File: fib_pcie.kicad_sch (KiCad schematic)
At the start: 57 parts, among them J901 Bus_M.2_2199230-6, J902 Bus_M.2_1-2199230-6, M901 Mech_M2_2280_H2.5mm, Y901 Oscillator_SMD_32.768kHz_ECS_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

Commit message: added some missing footprints, stared working ono power-on and sequencing
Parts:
- C917: value C_100n_0402 -> 100nF; footprint jetson-orin-baseboard-footprints:C_0402_1005Metric -> Capacitor_SMD:C_0603_1608Metric
- R913, R914, R919, R920, R921, R922, R923: footprint jetson-orin-baseboard-footprints:R_0402_1005Metric -> Resistor_SMD:R_0603_1608Metric
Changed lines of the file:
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@@
 			)
 		)
-		(property "Footprint" "jetson-orin-baseboard-footprints:R_0402_1005Metric"
+		(property "Footprint" "Resistor_SMD:R_0603_1608Metric"
 			(at 175.26 151.13 0)
 			(effects
@@
 			)
 		)
-		(property "Footprint" "jetson-orin-baseboard-footprints:R_0402_1005Metric"
+		(property "Footprint" "Resistor_SMD:R_0603_1608Metric"
 			(at 251.46 153.67 0)
 			(effects
@@
 			)
 		)
-		(property "Footprint" "jetson-orin-baseboard-footprints:R_0402_1005Metric"
+		(property "Footprint" "Resistor_SMD:R_0603_1608Metric"
 			(at 175.26 158.75 0)
 			(effects
@@
 			)
 		)
-		(property "Footprint" "jetson-orin-baseboard-footprints:R_0402_1005Metric"
+		(property "Footprint" "Resistor_SMD:R_0603_1608Metric"
 			(at 175.26 146.05 0)
 			(effects
@@
 			)
 		)
-		(property "Footprint" "jetson-orin-baseboard-footprints:R_0402_1005Metric"
+		(property "Footprint" "Resistor_SMD:R_0603_1608Metric"
 			(at 251.46 163.83 0)
 			(effects
@@
 			)
 		)
-		(property "Footprint" "jetson-orin-baseboard-footprints:R_0402_1005Metric"
+		(property "Footprint" "Resistor_SMD:R_0603_1608Metric"
 			(at 175.26 148.59 0)
 			(effects
@@
 			)
 		)
-		(property "Footprint" "jetson-orin-baseboard-footprints:R_0402_1005Metric"
+		(property "Footprint" "Resistor_SMD:R_0603_1608Metric"
 			(at 251.46 158.75 0)
 			(effects
@@
 			)
 		)
-		(property "Value" "C_100n_0402"
+		(property "Value" "100nF"
 			(at 34.29 176.53 0)
 			(effects
@@
 			)
 		)
-		(property "Footprint" "jetson-orin-baseboard-footprints:C_0402_1005Metric"
+		(property "Footprint" "Capacitor_SMD:C_0603_1608Metric"
 			(at 36.83 176.53 0)
 			(effects

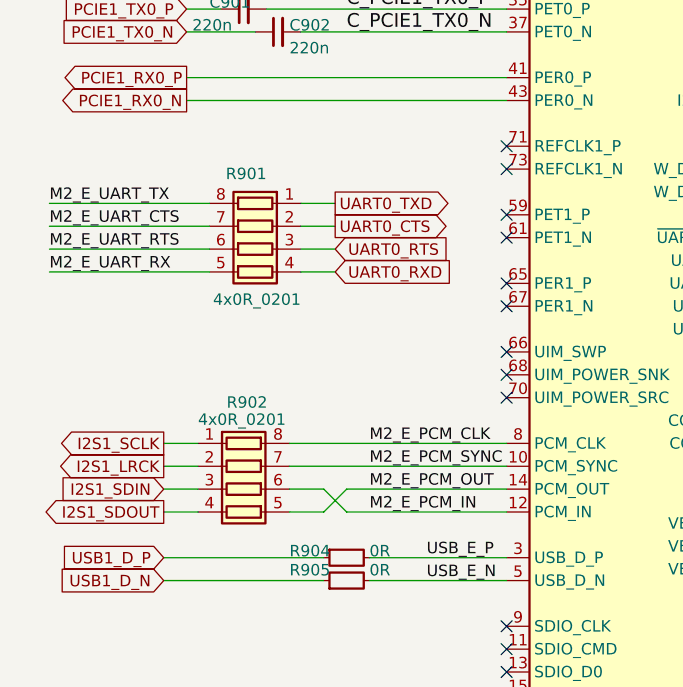
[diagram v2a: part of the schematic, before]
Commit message: implemented most of USB and Power Supplies
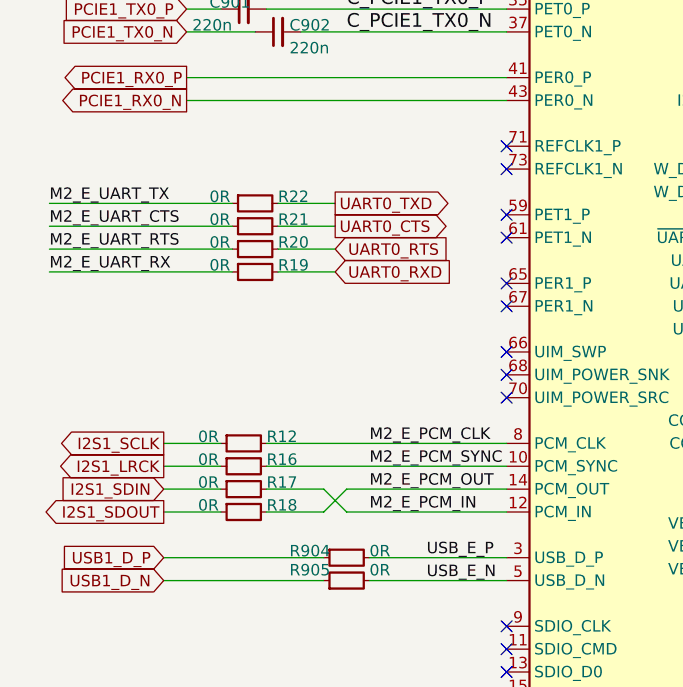
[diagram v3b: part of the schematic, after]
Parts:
- removed R901, R902: R_4x0R_0201_array, jetson-orin-baseboard-footprints:R_Array_4x0201_Panasonic_EXB18V, symbol jetson-orin-baseboard:R_4x0R_0201_array
- added R12, R16, R17, R18, R19, R20, R21, R22: R_0R_0402, Resistor_SMD:R_0402_1005Metric, symbol jetson-orin-baseboard:R_0R_0402
- C901, C902, C905, C906, C907, C908, C909, C910, C911, C912, C917: footprint Capacitor_SMD:C_0603_1608Metric -> Capacitor_SMD:C_0402_1005Metric
- R903, R904, R905, R906, R907, R908, R909, R910, R911, R912, R913, R914, R915, R916, R917, R918, R919, R920, R921, R922, R923: footprint Resistor_SMD:R_0603_1608Metric -> Resistor_SMD:R_0402_1005Metric
- TP901, TP902, TP903, TP904, TP905, TP906, TP907: footprint TestPoint:TestPoint_Pad_D1.0mm -> (none)
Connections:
- net I2S1_LRCK: now also R16.1
- net I2S1_SCLK: now also R12.1
- net I2S1_SDIN: now also R17.1
- net I2S1_SDOUT: now also R18.1
- net M2_E_PCM_CLK: now also R12.2
- net M2_E_PCM_IN: now also R17.2
- net M2_E_PCM_OUT: now also R18.2
- net M2_E_PCM_SYNC: now also R16.2
- net M2_E_UART_CTS: now also R21.1
- net M2_E_UART_RTS: now also R20.1
- net M2_E_UART_RX: now also R19.1
- net M2_E_UART_TX: now also R22.1
- net UART0_CTS: now also R21.2
- net UART0_RTS: now also R20.2
- net UART0_RXD: now also R19.2
- net UART0_TXD: now also R22.2

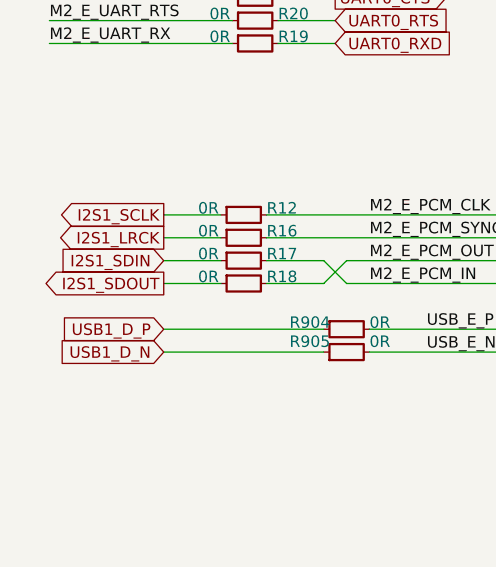
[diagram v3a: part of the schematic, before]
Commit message: did a big portion of pcie, optimized placement of components and subsections. power, usb and charging is largely done. still need to do length matching though. will need to take a second look at schemativs after routing is done
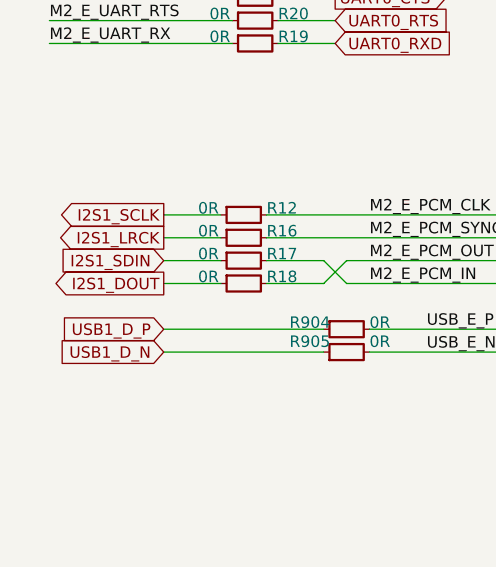
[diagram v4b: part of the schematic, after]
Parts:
- J901: footprint jetson-orin-baseboard-footprints:Bus_M.2_Socket_Key_E_TE_2199230-6 -> Fibel2:21992306; symbol jetson-orin-baseboard:Bus_M.2_2199230-6 -> Fibel2:Bus_M.2_2199230-6
- J902: footprint jetson-orin-baseboard-footprints:Bus_M.2_Socket_Key_M_TE_1-2199230-6 -> Fibel2:121992306; symbol jetson-orin-baseboard:Bus_M.2_1-2199230-6 -> Fibel2:Bus_M.2_1-2199230-6
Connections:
- net I2S1_SDOUT renamed I2S1_DOUT
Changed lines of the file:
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@@
 		)
 	)
-	(global_label "I2S1_SDOUT"
+	(global_label "I2S1_DOUT"
 		(shape output)
 		(at 30.48 105.41 180)
@@
 	)
 	(symbol
-		(lib_id "jetson-orin-baseboard:Bus_M.2_2199230-6")
+		(lib_id "Fibel2:Bus_M.2_2199230-6")
 		(at 68.58 31.75 0)
 		(unit 1)
@@
 			)
 		)
-		(property "Footprint" "jetson-orin-baseboard-footprints:Bus_M.2_Socket_Key_E_TE_2199230-6"
+		(property "Footprint" "Fibel2:21992306"
 			(at 114.3 38.1 0)
 			(effects
@@
 	)
 	(symbol
-		(lib_id "jetson-orin-baseboard:Bus_M.2_1-2199230-6")
+		(lib_id "Fibel2:Bus_M.2_1-2199230-6")
 		(at 200.66 38.1 0)
 		(unit 1)
@@
 			)
 		)
-		(property "Footprint" "jetson-orin-baseboard-footprints:Bus_M.2_Socket_Key_M_TE_1-2199230-6"
+		(property "Footprint" "Fibel2:121992306"
 			(at 246.38 48.26 0)
 			(effects

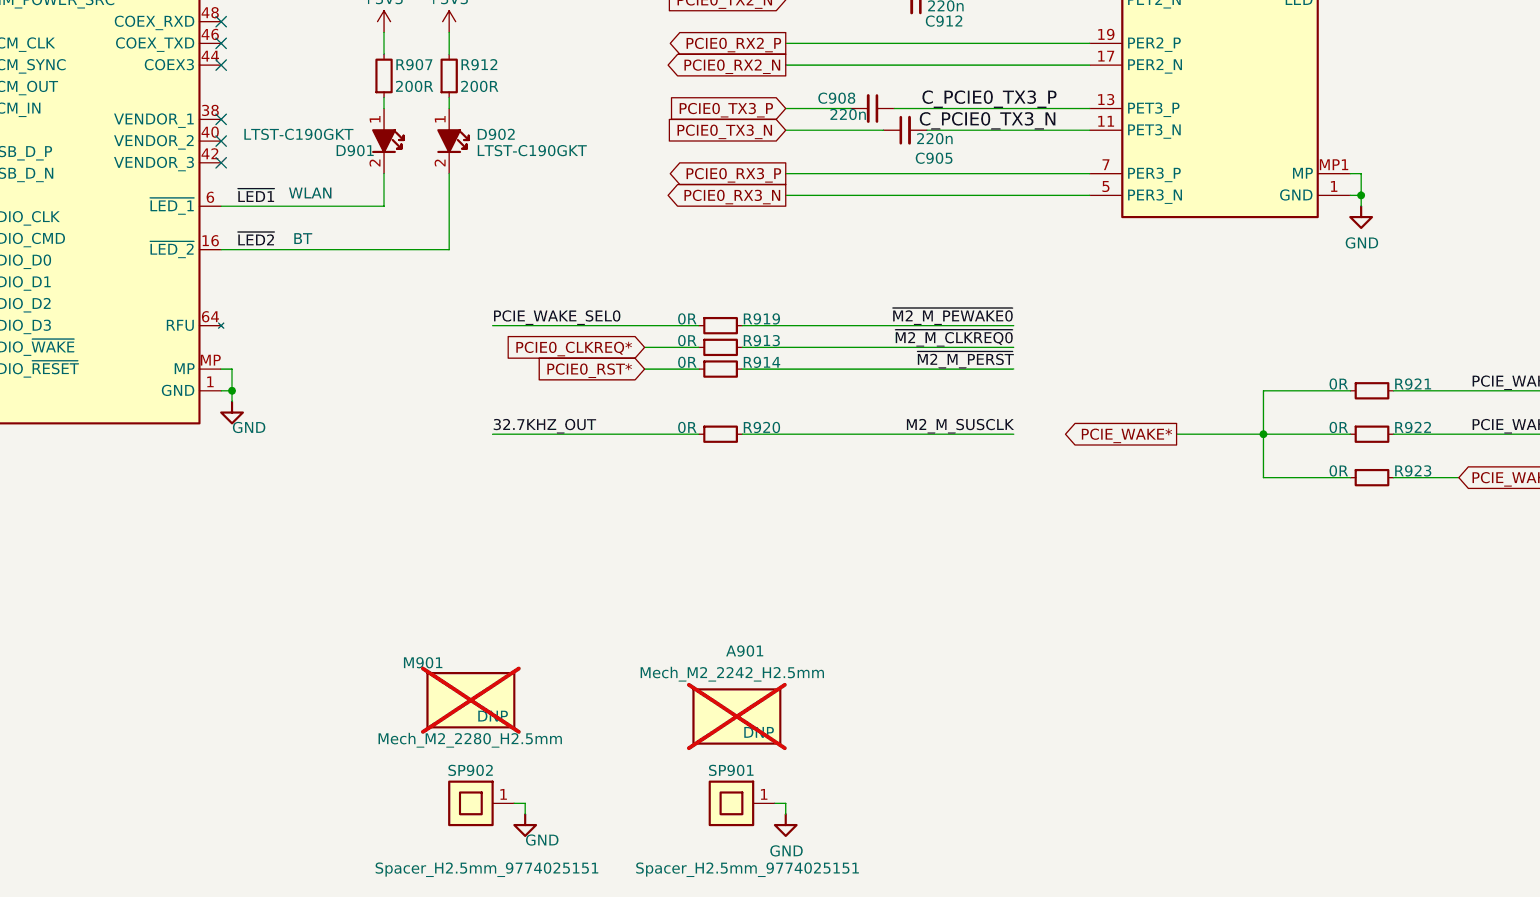
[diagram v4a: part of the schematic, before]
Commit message: further optimized placement, finished most of buck array, expanded pcie, added tons of missing footprints, diff pair spacing optimization
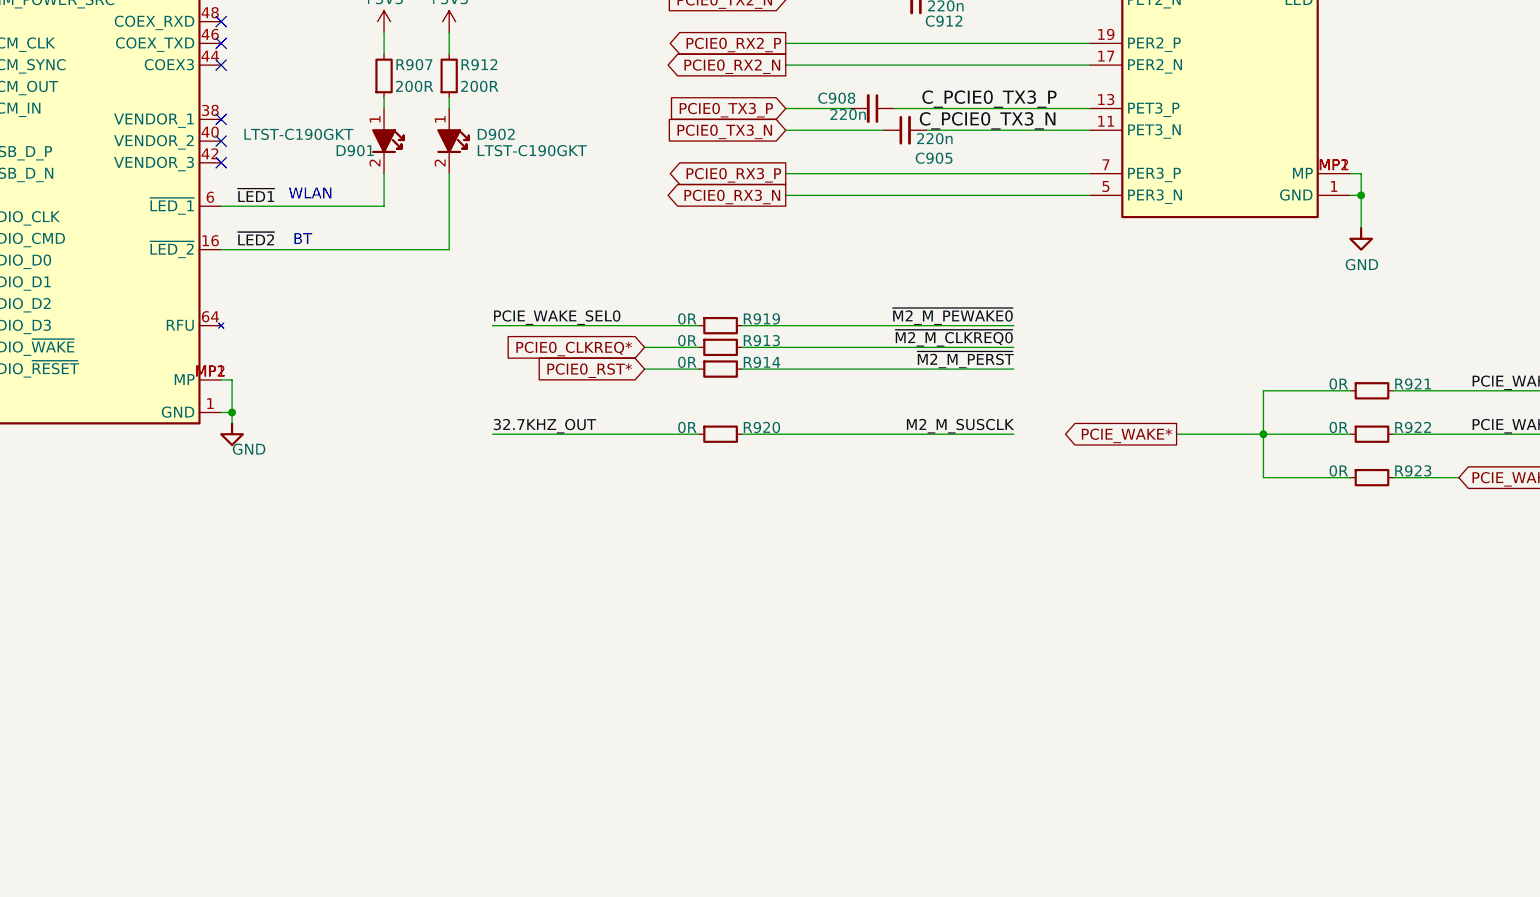
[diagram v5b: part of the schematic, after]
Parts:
- removed A901: Mech_M2_2242_H2.5mm, jetson-orin-baseboard-footprints:Mech_M2_2242_H2.5mm, symbol jetson-orin-baseboard:Mech_M2_2242_H2.5mm
- removed M901: Mech_M2_2280_H2.5mm, jetson-orin-baseboard-footprints:Mech_M2_2280_H2.5mm, symbol jetson-orin-baseboard:Mech_M2_2280_H2.5mm
- removed SP901, SP902: Spacer_H2.5mm_9774025151, jetson-orin-baseboard-footprints:Spacer_Drill3.7mm_H2.5mm_9774025151R, symbol jetson-orin-baseboard:Spacer_Drill3.7mm_H2.5mm_9774025151R
- D901, D902, D903: footprint jetson-orin-baseboard-footprints:LED_0603_1608Metric_G -> LED_SMD:LED_0603_1608Metric
- TP901, TP902, TP903, TP904, TP905, TP906, TP907: footprint (none) -> TestPoint:TestPoint_Pad_D1.0mm
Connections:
- net GND: now also J901.MP1 (MP), J901.MP2 (MP); no longer J901.MP

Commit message: 90 percent done with routing. need to go over all schematic pages, double check everything thoroughly, do lengthmatching add any missing footprints, take care of startup, ferrites, audio, eink connectors, 40pin header connections, rtc
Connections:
- net +3V3: no longer R917.2
- net 3V3_M2: now also R917.2
- net SYS_SCL renamed PCIE_SCL
- net SYS_SDA renamed PCIE_SDA
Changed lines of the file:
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@@
 	(wire
 		(pts
-			(xy 232.41 76.2) (xy 232.41 77.47)
+			(xy 232.41 74.93) (xy 232.41 77.47)
 		)
 		(stroke
@@
 		)
 	)
+	(label "3V3_M2"
+		(at 232.41 74.93 0)
+		(fields_autoplaced yes)
+		(effects
+			(font
+				(size 1.27 1.27)
+			)
+			(justify left bottom)
+		)
+	)
 	(label "PCIE_WAKE_SEL1"
 		(at 44.45 38.1 0)
@@
 		)
 	)
-	(global_label "SYS_SDA"
+	(global_label "PCIE_SDA"
 		(shape bidirectional)
 		(at 129.54 59.69 0)
@@
 		)
 	)
-	(global_label "SYS_SCL"
+	(global_label "PCIE_SCL"
 		(shape input)
 		(at 129.54 62.23 0)
@@
 					(unit 1)
 				)
-			)
-		)
-	)
-	(symbol
-		(lib_id "jetson-orin-baseboard:+3V3")
-		(at 232.41 76.2 0)
-		(unit 1)
-		(exclude_from_sim no)
-		(in_bom yes)
-		(on_board yes)
-		(dnp no)
-		(property "Reference" "#PWR0912"
-			(at 232.41 80.01 0)
-			(effects
-				(font
-					(size 1.27 1.27)
-				)
-				(justify left bottom)
-				(hide yes)
-			)
-		)
-		(property "Value" "+3V3"
-			(at 229.87 73.66 0)
-			(effects
-				(font
-					(size 1.27 1.27)
-				)
-				(justify left bottom)
-			)
-		)
-		(property "Footprint" ""
-			(at 232.41 76.2 0)
-			(effects
-				(font
-					(size 1.27 1.27)
-				)
-				(justify left bottom)
-				(hide yes)
-			)
-		)
-		(property "Datasheet" ""
-			(at 232.41 76.2 0)
-			(effects
-				(font
-					(size 1.27 1.27)
-				)
-				(justify left bottom)
-				(hide yes)
-			)
-		)
-		(property "Description" ""
-			(at 232.41 76.2 0)
-			(effects
-				(font
-					(size 1.27 1.27)
-				)
-				(hide yes)
-			)
-		)
-		(pin "1"
-		)
-		(instances
-			(project "Fibel2"
-				(path "/862c21e2-7ec9-4f80-a33c-aad02ea9423e/afa85234-73ed-4fc7-9570-87e781c133e5"
-					(reference "#PWR0912")
-					(unit 1)
-				)

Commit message: replaced 1v8 buck with ldo, added startup circuit, added footprints for eink connectors
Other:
- note removed: "Check if RX/TX needd too be swapped arouond"
- note removed: "NOTE: Place bulk caps near to the M.2 power pads"
- note removed: "PCIE_WAKE"
- note removed: "ROOT MODE"
- note removed: "SUSCLK"
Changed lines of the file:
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@@
-		)
-	)
-	(text "PCIE_WAKE"
-		(exclude_from_sim no)
-		(at 20.574 185.42 0)
-		(effects
-			(font
-				(size 1.27 1.27)
-			)
-		)
-	)
-	(text "SUSCLK"
-		(exclude_from_sim no)
-		(at 19.05 178.562 0)
-		(effects
-			(font
-				(size 1.27 1.27)
-			)
-		)
-	)
-	(text "Check if RX/TX needd too be swapped arouond\n"
-		(exclude_from_sim no)
-		(at 121.666 17.526 0)
-		(effects
-			(font
-				(size 1.27 1.27)
-			)
 		)
 	)
@@
 		(exclude_from_sim no)
 		(at 107.442 121.666 0)
-		(effects
-			(font
-				(size 1.27 1.27)
-			)
-			(justify left bottom)
-		)
-	)
-	(text "NOTE:\nPlace bulk caps near \nto the M.2 power pads"
-		(exclude_from_sim no)
-		(at 30.988 192.786 0)
-		(effects
-			(font
-				(size 1.27 1.27)
-			)
-			(justify left bottom)
-		)
-	)
-	(text "NOTE:\nPlace bulk caps near \nto the M.2 power pads"
-		(exclude_from_sim no)
-		(at 236.22 35.56 0)
 		(effects
 			(font
@@
 		)
 	)
-	(text "ROOT MODE"
-		(exclude_from_sim no)
-		(at 20.828 193.04 0)
-		(effects
-			(font
-				(size 1.27 1.27)
-			)
-		)
-	)
